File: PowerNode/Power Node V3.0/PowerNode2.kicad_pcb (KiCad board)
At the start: 2 copper layers, 78.4 x 64.8 mm, 42 parts, among them IC1 4511N, IC4 ACS712-LC, IC5 74595N, IC7 4511N

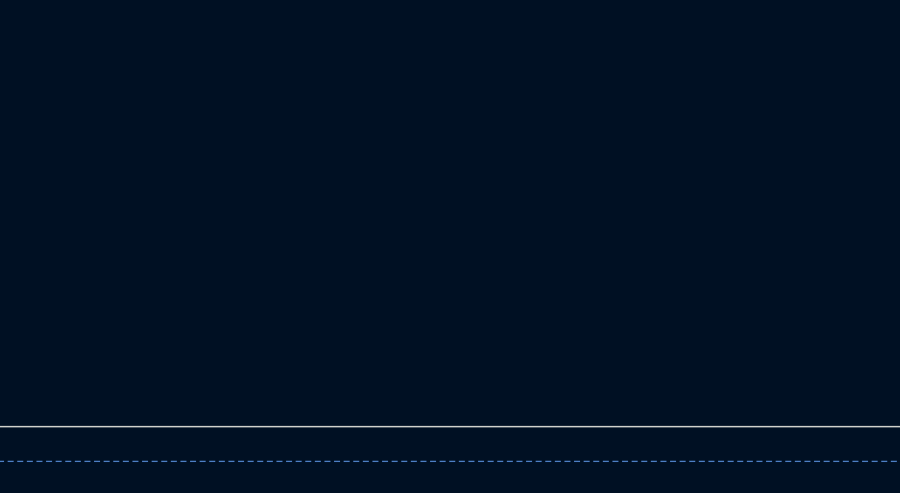
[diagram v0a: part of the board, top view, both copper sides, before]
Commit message: Power node 3.0 fixes, updates, and improvements
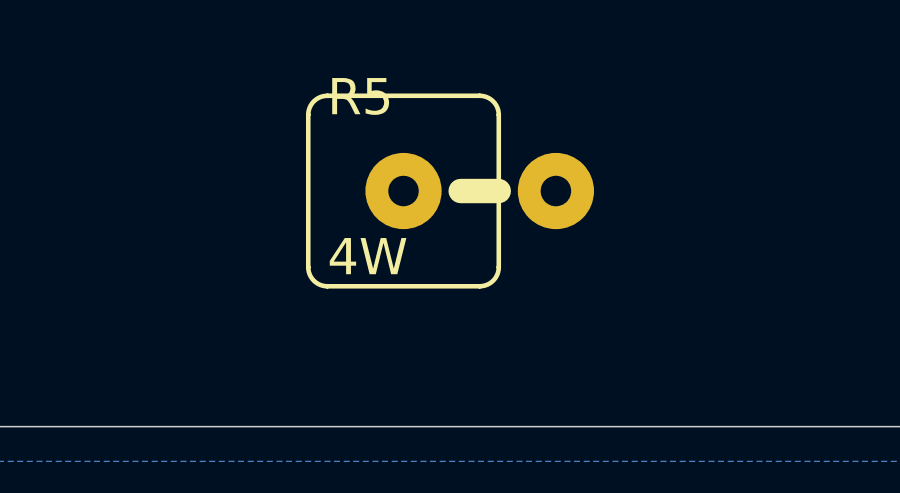
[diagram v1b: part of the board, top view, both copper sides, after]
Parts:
- added R5: 300k, PowerNode2:KH206-8R, F.Cu at (147.3, 64.8)
- IC5: value 74595N -> 74HC595N
- R2: value 1.2M -> 1.2Meg
- R7: value 330 -> 300k
- S1: value SWITCH-SPDT-PTH-11.6X4.0MM -> SW_SPDT
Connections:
- net VDD renamed Vdd
- net VSS renamed Vss
- C1 pad 2: Net-(C1-Pad2) -> /GND
- C2 pad 2: Net-(C1-Pad2) -> /GND
- GND1 pad 1: Net-(C1-Pad2) -> /GND
- GND2 pad 1: Net-(C1-Pad2) -> /GND
- GNDHIIN1 pad 1: Net-(C1-Pad2) -> /GND
- IC1 pad 5: Net-(C1-Pad2) -> /GND
- IC4 pad 1: Net-(C1-Pad2) -> /GND
- IC4 pad 2: Net-(C1-Pad2) -> /GND
- IC4 pad 5: Net-(C1-Pad2) -> /GND
- IC5 pad 13: Net-(C1-Pad2) -> /GND
- IC5 pad 8: Net-(C1-Pad2) -> /GND
- IC7 pad 5: Net-(C1-Pad2) -> /GND
- INOUT1 pad 2: Net-(C1-Pad2) -> /GND
- LED1 pad 3: Net-(C1-Pad2) -> /GND
- LED1 pad 8: Net-(C1-Pad2) -> /GND
- LED2 pad 3: Net-(C1-Pad2) -> /GND
- LED2 pad 8: Net-(C1-Pad2) -> /GND
- R1 pad 1: Net-(C1-Pad2) -> /GND
- R4 pad 1: Net-(C1-Pad2) -> /GND
- R4 pad 2: Net-(PWRLED1-PadK) -> Net-(PWRLED1-Pad1)
- R6 pad 1: Net-(C1-Pad2) -> /GND
- S1 pad 3: Net-(C1-Pad2) -> /GND
- U$1 pad 14: Net-(C1-Pad2) -> /GND
- U$1 pad 8: Net-(R3-PadS) -> Net-(R3-Pad2)
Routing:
- net Net-(R3-PadS): track 125.2 -> 0.00 mm, vias 2 -> 0
- net Net-(R3-Pad2): track 0.00 -> 125.2 mm, vias 0 -> 2
- net Net-(PWRLED1-PadK): track 19.9 -> 0.00 mm
- net Net-(PWRLED1-Pad1): track 0.00 -> 19.9 mm
- net Net-(C1-Pad2): track 11.0 -> 8.80 mm, vias 3 -> 2
- net /GND: track 0.00 -> 2.16 mm, vias 0 -> 1

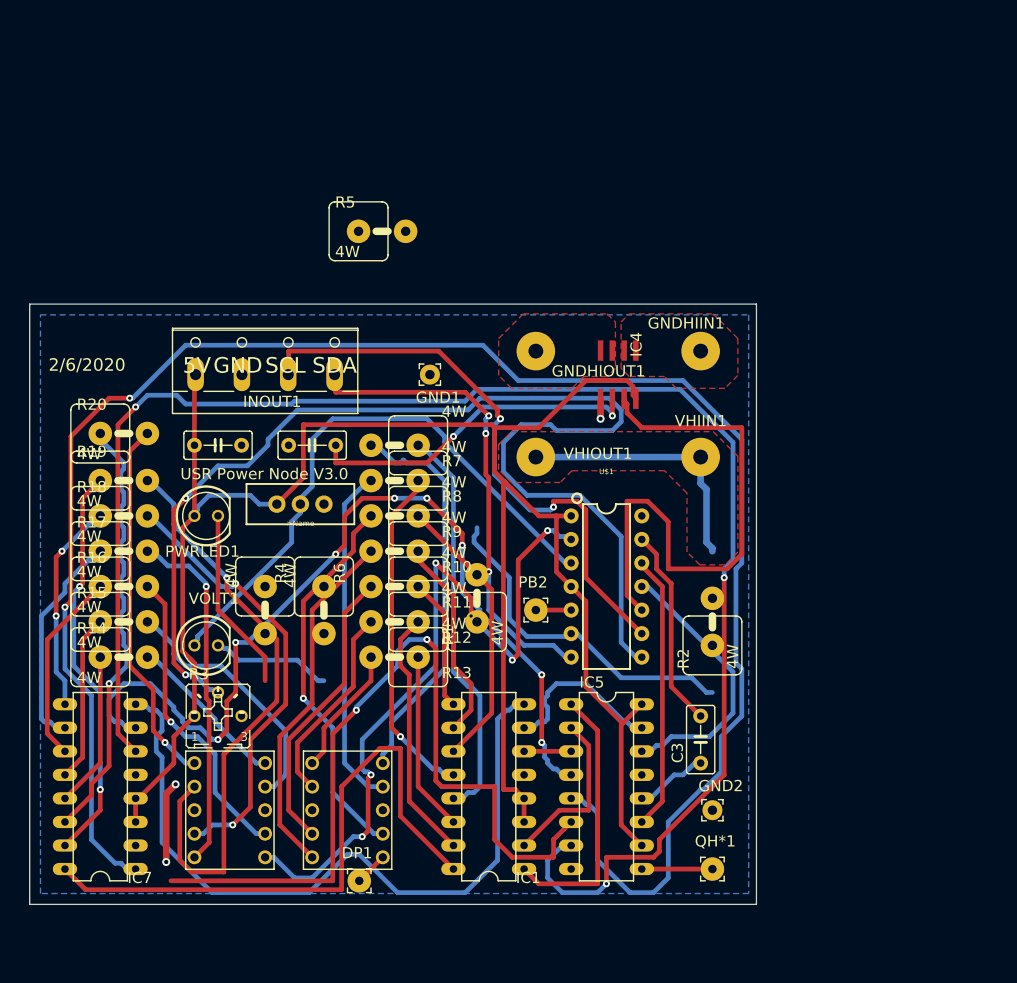
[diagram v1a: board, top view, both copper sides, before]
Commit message: Remapped PN3 footprints
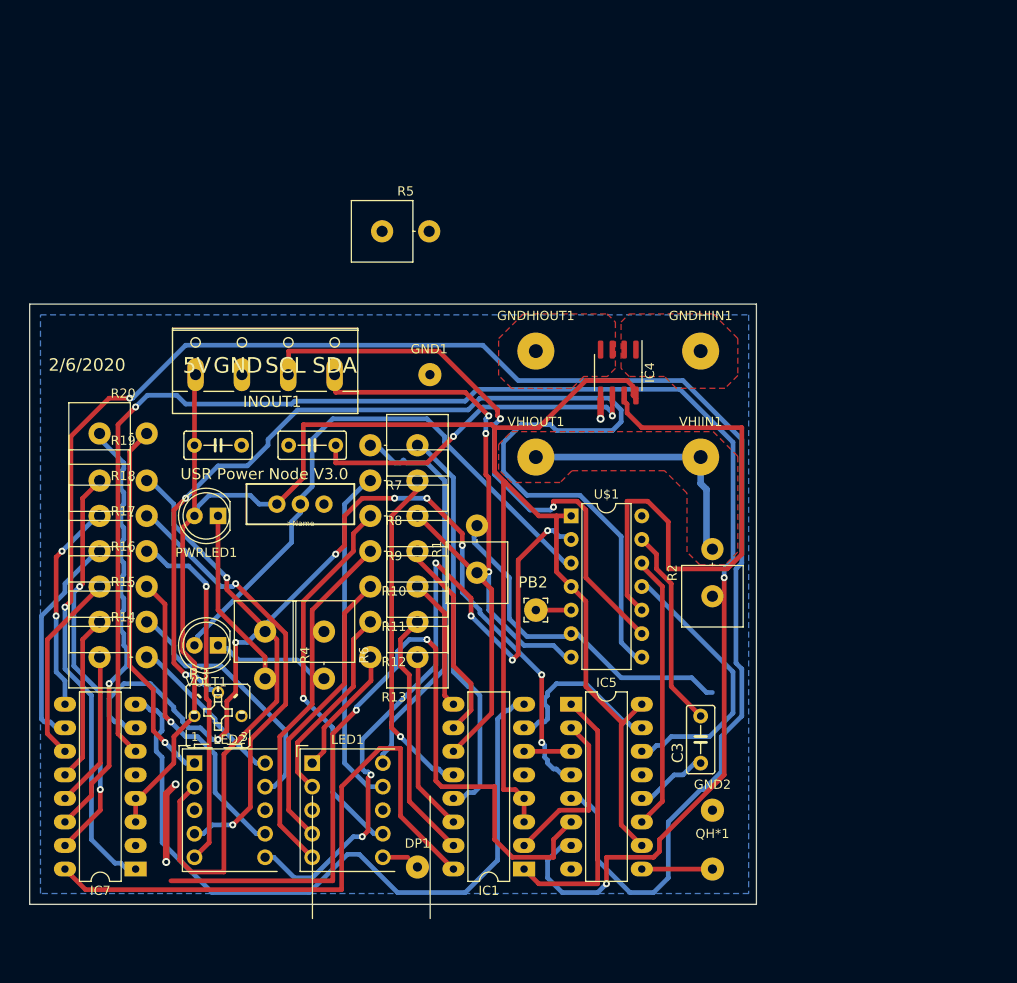
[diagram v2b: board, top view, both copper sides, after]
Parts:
- DP1, QH*1: footprint PowerNode2:2,54_0,9 -> Connector_Wire:SolderWirePad_1x01_Drill1mm
- GND1, GND2: footprint PowerNode2:2,15_1,0 -> Connector_Wire:SolderWirePad_1x01_Drill1mm
- GNDHIIN1, GNDHIOUT1, VHIIN1, VHIOUT1: footprint PowerNode2:4,16O1,6 -> Connector_Wire:SolderWirePad_1x01_Drill1.5mm
- IC1, IC5, IC7: footprint PowerNode2:DIL16 -> Package_DIP:DIP-16_W7.62mm_LongPads
- IC4: value ACS712-LC -> ACS712xLCTR-30A; footprint PowerNode2:SOIC8 -> Package_SO:SOIC-8_3.9x4.9mm_P1.27mm
- LED1, LED2: footprint PowerNode2:S4301B -> Display_7Segment:Sx39-1xxxxx
- PWRLED1, VOLT1: footprint PowerNode2:LED5MM -> LED_THT:LED_D5.0mm
- R1, R10, R11, R12, R13, R14, R15, R16, R17, R18, R19, R2, R20, R4, R5, R6, R7, R8, R9: footprint PowerNode2:KH206-8R -> Resistor_THT:R_Axial_Power_L20.0mm_W6.4mm_P5.08mm_Vertical
- U$1: value ATTINY84ATTINY84-20PU -> ATtiny84-20PU; footprint PowerNode2:DIP14 -> Package_DIP:DIP-14_W7.62mm
- moved DP1 6.45 mm to (151.1, 133.3)
- moved R1 2.76 mm to (157.6, 101.6)
- moved R2 2.76 mm to (183.0, 104.1)
- moved R14 2.62 mm to (116.8, 110.7)
- moved R15 2.62 mm to (116.8, 106.9)
- moved R16 2.62 mm to (116.8, 103.1)
- moved R17 2.62 mm to (116.8, 99.3)
- moved R18 2.62 mm to (116.8, 95.5)
- moved R19 2.62 mm to (116.8, 91.7)
- moved R20 2.62 mm to (116.8, 86.6)
- moved R10 2.46 mm to (151.1, 99.3)
- moved R11 2.46 mm to (151.1, 103.1)
- moved R12 2.46 mm to (151.1, 106.9)
- moved R13 2.46 mm to (151.1, 110.7)
- moved R7 2.46 mm to (151.1, 87.9)
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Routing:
- net Net-(DP1-Pad1): track 3.59 -> 4.17 mm

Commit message: PN3: updated PCB and added protective capacitors to VMEAS
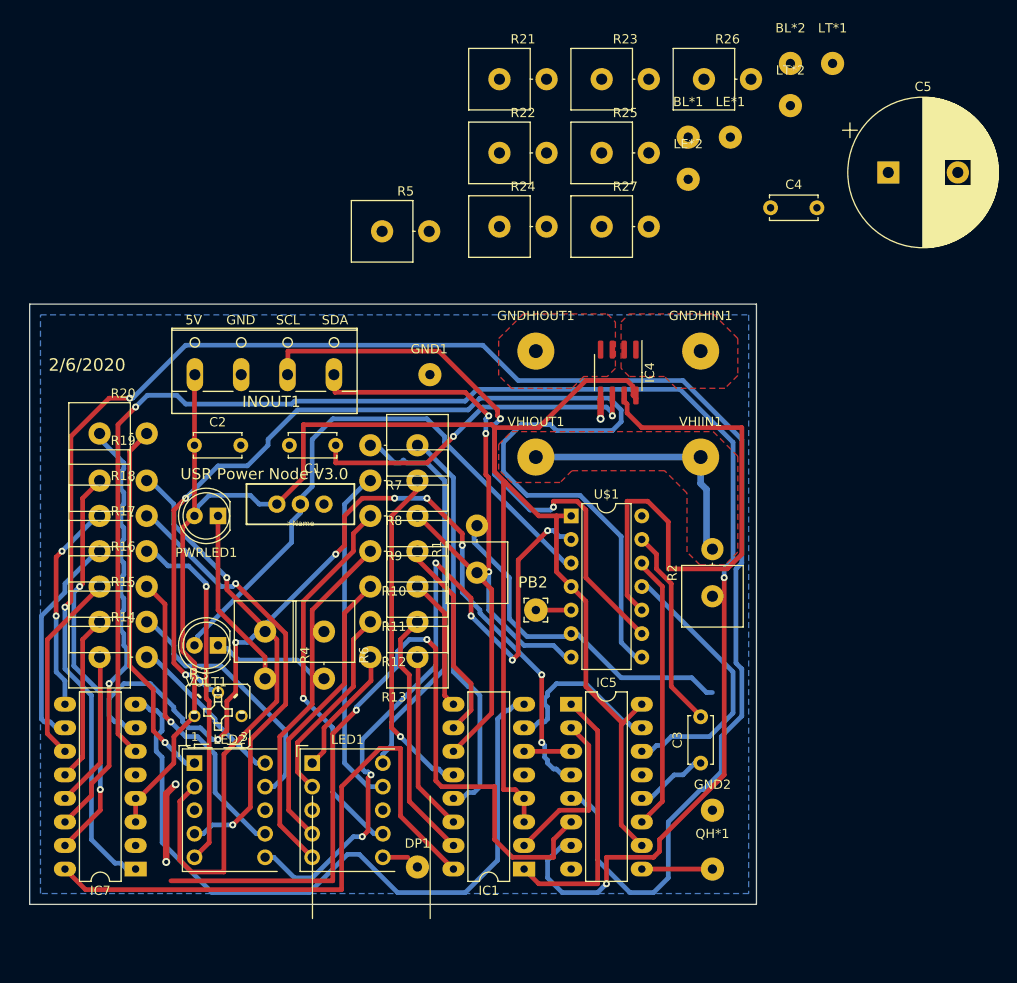
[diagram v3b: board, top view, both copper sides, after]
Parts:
- added BL*1: 2,54_0,9, Connector_Wire:SolderWirePad_1x01_Drill1mm, F.Cu at (180.3, 54.6)
- added BL*2: 2,54_0,9, Connector_Wire:SolderWirePad_1x01_Drill1mm, F.Cu at (191.4, 46.7)
- added C4: 0.1uF, Capacitor_THT:C_Disc_D5.0mm_W2.5mm_P5.00mm, F.Cu at (189.2, 62.2)
- added C5: 100uF, Capacitor_THT:CP_Radial_D16.0mm_P7.50mm, F.Cu at (201.9, 58.4)
- added LE*1: 2,54_0,9, Connector_Wire:SolderWirePad_1x01_Drill1mm, F.Cu at (184.9, 54.6)
- added LE*2: 2,54_0,9, Connector_Wire:SolderWirePad_1x01_Drill1mm, F.Cu at (180.3, 59.2)
- added LT*1: 2,54_0,9, Connector_Wire:SolderWirePad_1x01_Drill1mm, F.Cu at (195.9, 46.7)
- added LT*2: 2,54_0,9, Connector_Wire:SolderWirePad_1x01_Drill1mm, F.Cu at (191.4, 51.2)
- added R21: 10k, Resistor_THT:R_Axial_Power_L20.0mm_W6.4mm_P5.08mm_Vertical, F.Cu at (160.0, 48.4)
- added R22: 10k, Resistor_THT:R_Axial_Power_L20.0mm_W6.4mm_P5.08mm_Vertical, F.Cu at (160.0, 56.3)
- added R23: 10k, Resistor_THT:R_Axial_Power_L20.0mm_W6.4mm_P5.08mm_Vertical, F.Cu at (171.0, 48.4)
- added R24: 10k, Resistor_THT:R_Axial_Power_L20.0mm_W6.4mm_P5.08mm_Vertical, F.Cu at (160.0, 64.3)
- added R25: 10k, Resistor_THT:R_Axial_Power_L20.0mm_W6.4mm_P5.08mm_Vertical, F.Cu at (171.0, 56.3)
- added R26: 10k, Resistor_THT:R_Axial_Power_L20.0mm_W6.4mm_P5.08mm_Vertical, F.Cu at (182.0, 48.4)
- added R27: 220, Resistor_THT:R_Axial_Power_L20.0mm_W6.4mm_P5.08mm_Vertical, F.Cu at (171.0, 64.3)
- C1, C2, C3: footprint PowerNode2:C5B3 -> Capacitor_THT:C_Disc_D5.0mm_W2.5mm_P5.00mm
- IC1, IC7: value 4511N -> CD4511B
- LED1, LED2: value S4301B -> LTS-4301P
- R10, R11, R12, R13, R14, R15, R16, R17, R18, R19, R20, R5, R7, R8, R9: value 300k -> 220
- R4, R6: value 330 -> 220
- moved C3 2.54 mm to (181.7, 122.1)
- moved C1 2.54 mm to (142.3, 87.9)
- moved C2 2.54 mm to (127.1, 87.9)
- moved INOUT1 0.08 mm to (134.6, 79.0)
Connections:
- net Net-(IC4-Pad7) renamed /IMEAS
- net Net-(R1-Pad2) renamed /VMEAS
- net Net-(R2-Pad2) renamed /VHI
- net Net-(R3-Pad2) renamed /VPOT
- net Net-(S1-Pad2) renamed /SWITCH
- C1 pad 2: /GND -> GND
- C2 pad 1: /VCC -> Vdd
- C2 pad 2: /GND -> GND
- GND1 pad 1: /GND -> GND
- GND2 pad 1: /GND -> GND
- GNDHIIN1 pad 1: /GND -> GND
- IC1 pad 3: /VCC -> /LT*1
- IC1 pad 4: /VCC -> /BL*1
- IC1 pad 5: /GND -> /LE*1
- IC1 pad 8: Vss -> GND
- IC4 pad 1: /GND -> GND
- IC4 pad 2: /GND -> GND
- IC4 pad 5: /GND -> GND
- IC4 pad 8: /VCC -> Vdd
- IC5 pad 10: /VCC -> Vdd
- IC5 pad 13: /GND -> GND
- IC5 pad 16: /VCC -> Vdd
- IC5 pad 8: /GND -> GND
- IC7 pad 3: /VCC -> /LT*2
- IC7 pad 4: /VCC -> /BL*2
- IC7 pad 5: /GND -> /LE*2
- IC7 pad 8: Vss -> GND
- INOUT1 pad 1: /VCC -> Vdd
- INOUT1 pad 2: /GND -> GND
- LED1 pad 3: /GND -> GND
- LED1 pad 6: Net-(DP1-Pad1) -> Net-(LED1-Pad6)
- LED1 pad 8: /GND -> GND
- LED2 pad 3: /GND -> GND
- LED2 pad 8: /GND -> GND
- PWRLED1 pad 2: /VCC -> Vdd
- R1 pad 1: /GND -> GND
- R3 pad 1: /VCC -> Vdd
- R3 pad 3: /GND -> GND
- R4 pad 1: /GND -> GND
- R5 pad 1: Net-(R5-Pad1) -> Net-(LED2-Pad6)
- R6 pad 1: /GND -> GND
- S1 pad 1: /VCC -> Vdd
- S1 pad 3: /GND -> GND
- U$1 pad 1: /VCC -> Vdd
- U$1 pad 14: /GND -> GND
- U$1 pad 2: Net-(LED2-Pad6) -> Net-(R5-Pad2)
- U$1 pad 4: /VCC -> Vdd
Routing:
- net GND: track 0.00 -> 81.8 mm, vias 0 -> 1
- net Vss: track 79.6 -> 0.00 mm
- net /GND: track 2.16 -> 0.00 mm, vias 1 -> 0
- added copper zone on F.Cu, net Net-(R2-Pad2)
- removed copper zone on F.Cu, net /VHI
